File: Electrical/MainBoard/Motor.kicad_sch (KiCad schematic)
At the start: 44 parts, among them M1 Motor_DC, U1 DRV8842PWPR, U11 Quad_Encoder, U12 Quad_Encoder

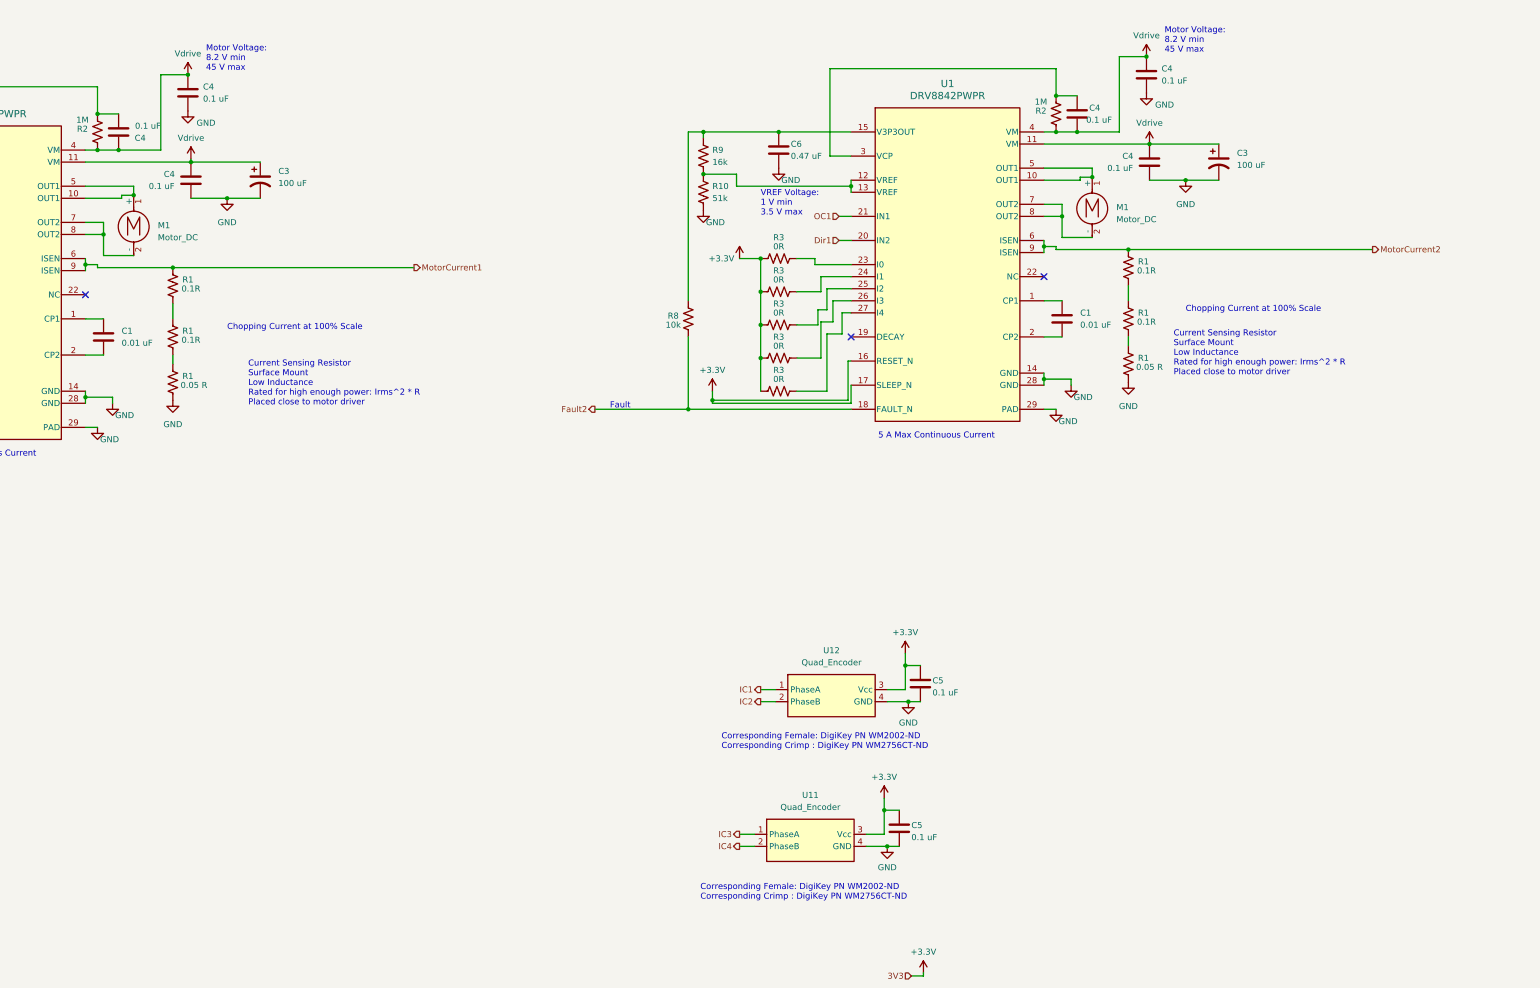
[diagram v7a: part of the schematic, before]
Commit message: Change molex+terminal block to just 6 position molex for the motor/encoder terminal
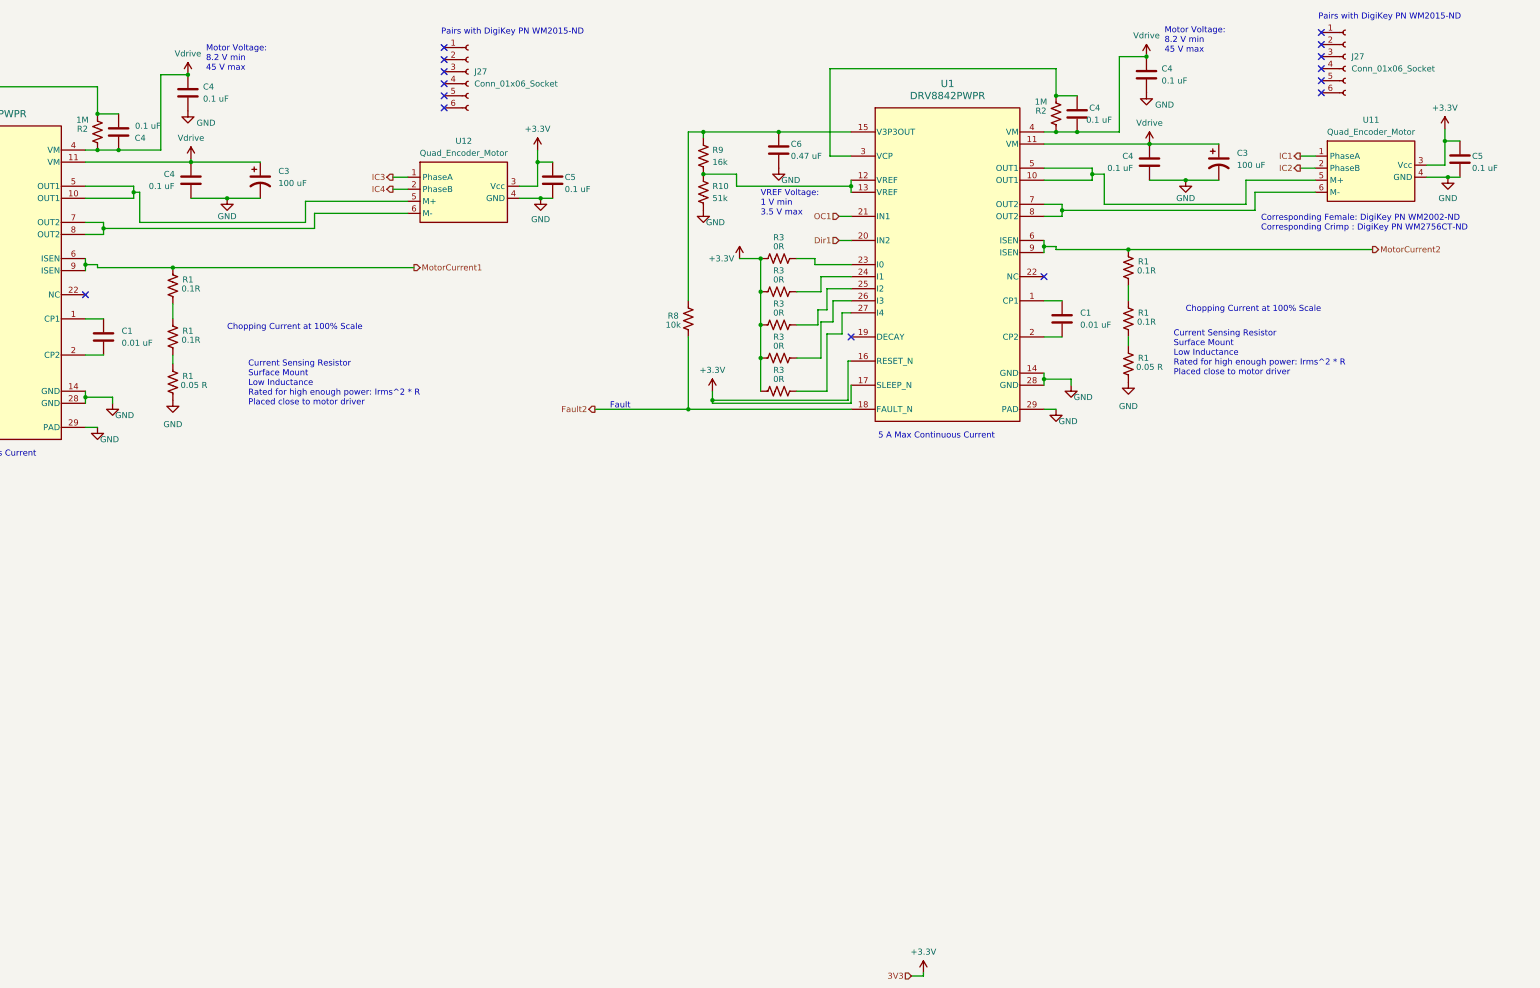
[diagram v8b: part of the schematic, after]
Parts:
- removed M1 (x2): Motor_DC, RobotLibrary:CONN_1890963_PXC, symbol Motor:Motor_DC
- removed U11, U12: Quad_Encoder, RobotLibrary:CONN_22-23-2041_MOL, symbol RobotLibary:Quadrature_Encoder
- added J27 (x2): Conn_01x06_Socket, symbol Connector:Conn_01x06_Socket
- added U11, U12: Quad_Encoder_Motor, Connector_Molex:Molex_KK-254_AE-6410-06A_1x06_P2.54mm_Vertical, symbol RobotLibary:Quadrature_Encoder_With_Motor
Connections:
- net +3.3V: now also U11.3 (Vcc), U12.3 (Vcc)
- net GND: now also U11.4 (GND), U12.4 (GND)
- net IC1: now also U11.1 (PhaseA)
- net IC2: now also U11.2 (PhaseB)
- net IC3: now also U12.1 (PhaseA)
- net IC4: now also U12.2 (PhaseB)
- net at U1.10 (OUT1), U1.5 (OUT1): now also U11.5 (M+)
- net at U1.7 (OUT2), U1.8 (OUT2): now also U11.6 (M-)
- net at U1.10 (OUT1), U1.5 (OUT1): now also U12.5 (M+)
- net at U1.7 (OUT2), U1.8 (OUT2): now also U12.6 (M-)
- no-connect marks 4 -> 16
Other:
- note added: "Pairs with DigiKey PN WM2015-ND"
- moved on the sheet: C5
